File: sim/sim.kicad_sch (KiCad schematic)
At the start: 25 parts, among them Q1 BC817, Q2 BC807, Q3 BUK7880-55A, U1 AD8051, U2 AD8051, U3 LM393

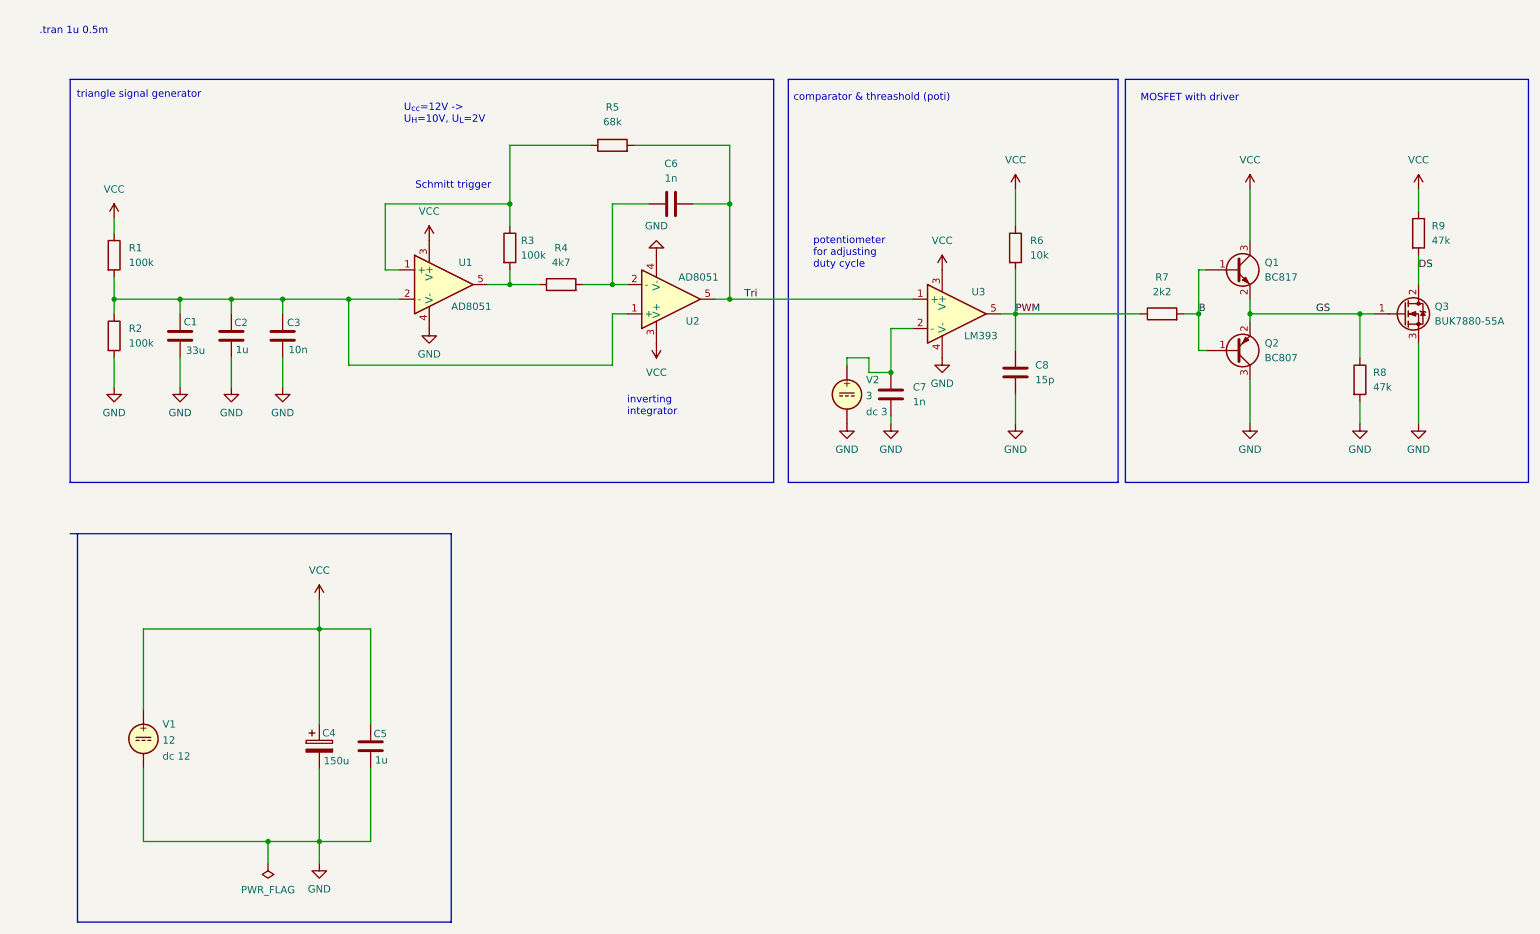
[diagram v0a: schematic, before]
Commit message: simulation model error fix
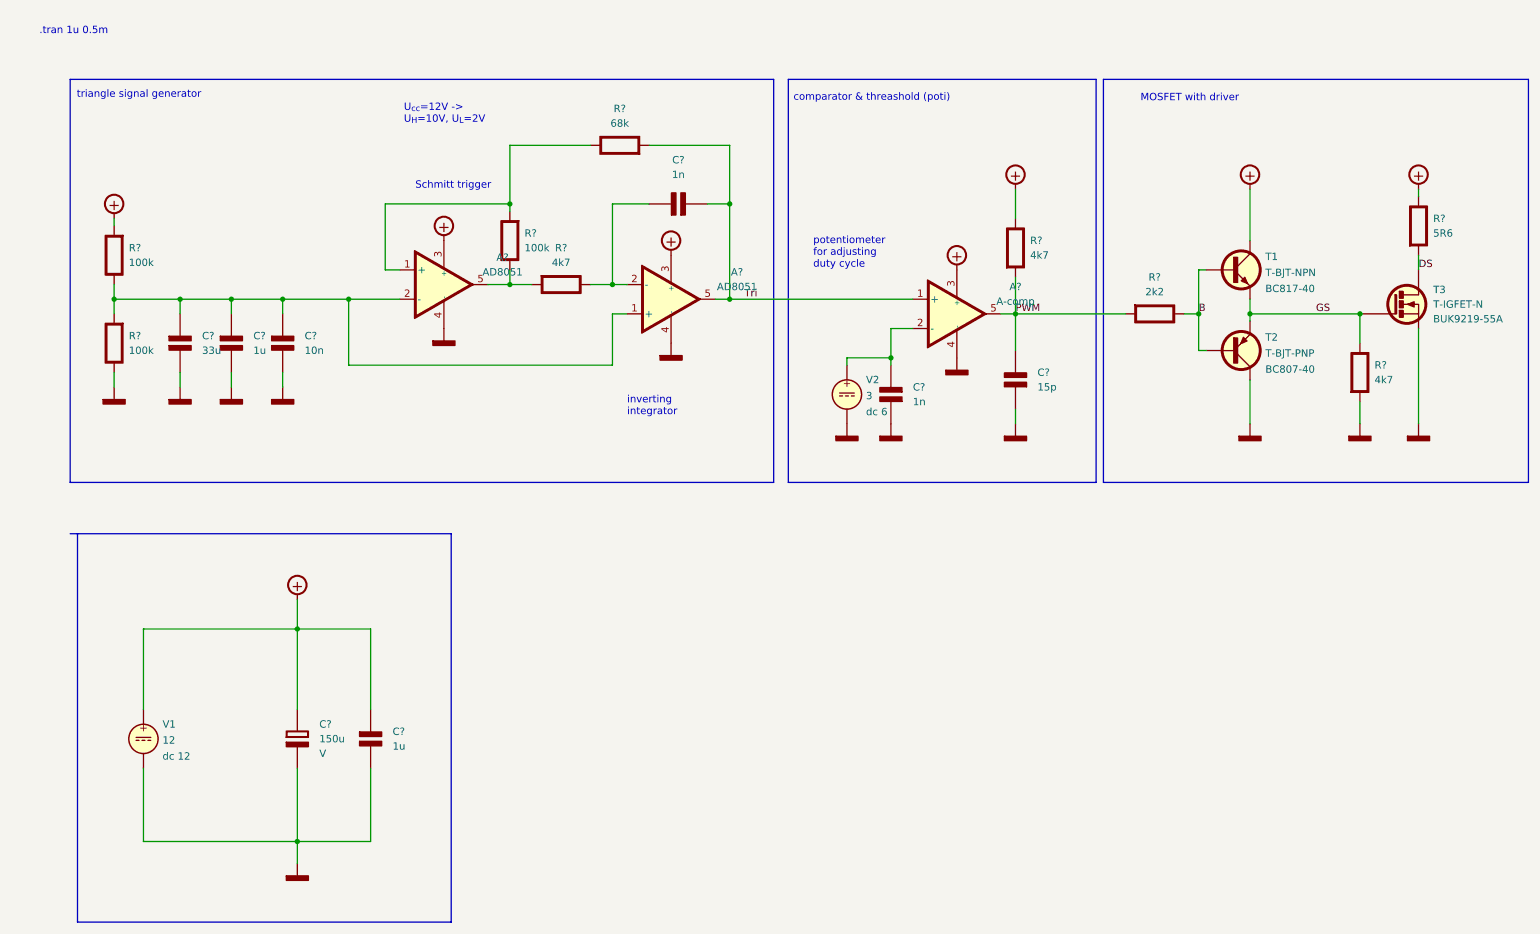
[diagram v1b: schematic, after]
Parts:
- removed C1: 33u, Capacitor_SMD:C_1206_3216Metric_Pad1.33x1.80mm_HandSolder, symbol Device:C
- removed C2, C5: 1u, Capacitor_SMD:C_1206_3216Metric_Pad1.33x1.80mm_HandSolder, symbol Device:C
- removed C3: 10n, Capacitor_SMD:C_1206_3216Metric_Pad1.33x1.80mm_HandSolder, symbol Device:C
- removed C4: 150u, Capacitor_THT:CP_Radial_D6.3mm_P2.50mm, symbol Device:C_Polarized
- removed C6, C7: 1n, Capacitor_SMD:C_1206_3216Metric_Pad1.33x1.80mm_HandSolder, symbol Device:C
- removed C8: 15p, Capacitor_SMD:C_1206_3216Metric_Pad1.33x1.80mm_HandSolder, symbol Device:C
- removed Q1: BC817, Package_TO_SOT_SMD:SOT-23, symbol Transistor_BJT:BC817
- removed Q2: BC807, Package_TO_SOT_SMD:SOT-23, symbol Transistor_BJT:BC807
- removed Q3: BUK7880-55A, Package_TO_SOT_SMD:SOT-223-3_TabPin2, symbol Transistor_FET:BUK7880-55A
- removed R1, R2, R3: 100k, Resistor_SMD:R_1206_3216Metric_Pad1.30x1.75mm_HandSolder, symbol Device:R
- removed R4: 4k7, Resistor_SMD:R_1206_3216Metric_Pad1.30x1.75mm_HandSolder, symbol Device:R
- removed R5: 68k, Resistor_SMD:R_1206_3216Metric_Pad1.30x1.75mm_HandSolder, symbol Device:R
- removed R6: 10k, Resistor_SMD:R_1206_3216Metric_Pad1.30x1.75mm_HandSolder, symbol Device:R
- removed R7: 2k2, Resistor_SMD:R_1206_3216Metric_Pad1.30x1.75mm_HandSolder, symbol Device:R
- removed R8, R9: 47k, Resistor_SMD:R_1206_3216Metric_Pad1.30x1.75mm_HandSolder, symbol Device:R
- removed U1, U2: AD8051, symbol sallen_key_schlib:Generic_Opamp
- removed U3: LM393, symbol sallen_key_schlib:Generic_Opamp
- added A?: A-comp, symbol Elektuur:A-comp
- added A?: AD8051, symbol Elektuur:A-comp
- added A?: AD8051, symbol Elektuur:A-opamp
- added C?: 15p, symbol Elektuur:C
- added C? (x2): 1u, symbol Elektuur:C
- added C? (x2): 1n, symbol Elektuur:C
- added C?: 150u, symbol Elektuur:C-polar
- added C?: 33u, symbol Elektuur:C
- added C?: 10n, symbol Elektuur:C
- added R? (x3): 100k, symbol Elektuur:R
- added R?: 5R6, symbol Elektuur:R
- added R? (x3): 4k7, symbol Elektuur:R
- added R?: 68k, symbol Elektuur:R
- added R?: 2k2, symbol Elektuur:R
- added T1: T-BJT-NPN, symbol Elektuur:T-BJT-NPN
- added T2: T-BJT-PNP, symbol Elektuur:T-BJT-PNP
- added T3: T-IGFET-N, symbol Elektuur:T-IGFET-N
- V2: Spice_Model dc 3 -> dc 6
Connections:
- net B: now also R?.1 (+), T1.2 (B), T2.2 (B)
- net DS: now also R?.2 (-), T3.1 (D)
- net GS: now also R?.1 (+), T1.3 (E), T2.3 (E), T3.2 (G)
- net PWM: now also A?.5 (OUT), C?.2 (-), R?.2 (-), R?.2 (-)
- net Tri: now also A?.1 (+), A?.5 (OUT), C?.2 (-), R?.2 (-)
- net at V2.1: now also A?.2 (-), C?.2 (-)
- net GND renamed 0
- net 0: now also A?.4 (-), A?.4 (-), A?.4 (-), C?.1 (+), C?.1 (+), C?.2 (-), C?.2 (-), C?.2 (-), C?.2 (-), C?.2 (-), R?.1 (+), R?.2 (-), T2.1 (C), T3.3 (S)
- net VCC renamed +
- net +: now also A?.3 (+), A?.3 (+), A?.3 (+), C?.1 (+), C?.1 (+), R?.1 (+), R?.1 (+), R?.2 (-), T1.1 (C)
- new net: A?.1 (+), A?.2 (-), C?.1 (+), C?.1 (+), C?.1 (+), R?.1 (+), R?.2 (-)
- new net: A?.2 (-), C?.1 (+), R?.1 (+)
- new net: A?.5 (OUT), R?.1 (+), R?.2 (-)
- new net: A?.1 (+), R?.1 (+), R?.2 (-)

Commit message: cleaning
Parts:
- R6: renamed from R?; value 4k7 -> 4k9
- V1: Spice_Model dc 12 -> dc 12 ac 0
- V2: value 3 -> 6; Spice_Model dc 6 -> dc 6 ac 0
- gave numbers to parts that had none: 19
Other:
- note added: ".tran 1u 0.5m .options gmin=1e-10 .options abstol=1e-10 .options reltol=0.003 .options cshunt=1e-15"
- note removed: ".tran 1u 0.5m"
- company: (none) -> Cherrytree
- title: (none) -> PWM generator simulation
- moved on the sheet: C6, C7, V2

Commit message: some more simulation stuff
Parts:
- A1, A2: value AD8051 -> TLV2371
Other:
- moved on the sheet: R6
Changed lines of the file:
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@@
   (junction (at 100.33 62.23) (diameter 0) (color 0 0 0 0)
   )
-  (junction (at 100.33 48.26) (diameter 0) (color 0 0 0 0)
+  (junction (at 100.33 38.1) (diameter 0) (color 0 0 0 0)
   )
   (junction (at 228.6 67.31) (diameter 0) (color 0 0 0 0)
@@
     (stroke (width 0) (type default) (color 0 0 0 0))
   )
-  (wire (pts (xy 100.33 48.26) (xy 78.74 48.26))
+  (wire (pts (xy 100.33 38.1) (xy 78.74 38.1))
     (stroke (width 0) (type default) (color 0 0 0 0))
   )
@@
     (stroke (width 0) (type default) (color 0 0 0 0))
   )
-  (wire (pts (xy 187.96 45.72) (xy 187.96 50.8))
+  (wire (pts (xy 187.96 45.72) (xy 187.96 46.99))
     (stroke (width 0) (type default) (color 0 0 0 0))
   )
@@
     (stroke (width 0) (type default) (color 0 0 0 0))
   )
-  (wire (pts (xy 100.33 49.53) (xy 100.33 48.26))
+  (wire (pts (xy 100.33 49.53) (xy 100.33 38.1))
     (stroke (width 0) (type default) (color 0 0 0 0))
   )
@@
     (stroke (width 0) (type default) (color 0 0 0 0))
   )
-  (wire (pts (xy 100.33 38.1) (xy 100.33 48.26))
-    (stroke (width 0) (type default) (color 0 0 0 0))
-  )
   (polyline (pts (xy 146.05 26.67) (xy 146.05 96.52))
     (stroke (width 0) (type default) (color 0 0 0 0))
@@
     (stroke (width 0) (type default) (color 0 0 0 0))
   )
-  (wire (pts (xy 78.74 48.26) (xy 78.74 59.69))
-    (stroke (width 0) (type default) (color 0 0 0 0))
-  )
-  (wire (pts (xy 187.96 60.96) (xy 187.96 67.31))
+  (wire (pts (xy 78.74 38.1) (xy 78.74 59.69))
+    (stroke (width 0) (type default) (color 0 0 0 0))
+  )
+  (wire (pts (xy 187.96 57.15) (xy 187.96 67.31))
     (stroke (width 0) (type default) (color 0 0 0 0))
   )
@@
     (effects (font (size 1.27 1.27)) (justify left bottom))
   )
-  (text "Schmitt trigger" (at 83.947 45.847 0)
+  (text "Schmitt trigger" (at 82.55 45.72 0)
     (effects (font (size 1.27 1.27)) (justify left bottom))
   )
@@
   )
   (symbol (lib_id "Elektuur:A-comp") (at 177.8 67.31 0) (unit 1)
-    (in_bom yes) (on_board yes) (fields_autoplaced)
-    (property "Reference" "A3" (id 0) (at 187.96 62.611 0))
-    (property "Value" "A-comp" (id 1) (at 187.96 65.151 0))
+    (in_bom yes) (on_board yes)
+    (property "Reference" "A3" (id 0) (at 184.15 69.85 0))
+    (property "Value" "A-comp" (id 1) (at 182.88 72.39 0))
     (property "Footprint" "" (id 2) (at 177.8 67.31 0)
       (effects (font (size 1.27 1.27)) hide)
@@
       (effects (font (size 1.27 1.27)) (justify left) hide)
     )
-    (property "Spice_Model" "LM393" (id 5) (at 177.8 67.31 0)
-      (effects (font (size 1.27 1.27)) hide)
-    )
+    (property "Spice_Model" "LM393" (id 5) (at 177.8 67.31 0))
     (property "Spice_Netlist_Enabled" "Y" (id 6) (at 177.8 67.31 0)
       (effects (font (size 1.27 1.27)) hide)
@@
   )
   (symbol (lib_id "Elektuur:A-comp") (at 88.9 62.23 0) (unit 1)
-    (in_bom yes) (on_board yes) (fields_autoplaced)
-    (property "Reference" "A1" (id 0) (at 99.06 57.531 0))
-    (property "Value" "AD8051" (id 1) (at 99.06 60.071 0))
+    (in_bom yes) (on_board yes)
+    (property "Reference" "A1" (id 0) (at 95.25 64.77 0))
+    (property "Value" "TLV2371" (id 1) (at 95.25 67.31 0))
     (property "Footprint" "" (id 2) (at 88.9 62.23 0)
       (effects (font (size 1.27 1.27)) hide)
@@
       (effects (font (size 1.27 1.27)) (justify left) hide)
     )
-    (property "Spice_Model" "AD8051" (id 5) (at 88.9 62.23 0)
-      (effects (font (size 1.27 1.27)) hide)
-    )
+    (property "Spice_Model" "AD8051" (id 5) (at 88.9 62.23 0))
     (property "Spice_Netlist_Enabled" "Y" (id 6) (at 88.9 62.23 0)
       (effects (font (size 1.27 1.27)) hide)
@@
     (pin "0")
   )
-  (symbol (lib_id "Elektuur:R") (at 187.96 55.88 0) (unit 1)
-    (in_bom yes) (on_board yes) (fields_autoplaced)
-    (property "Reference" "R6" (id 0) (at 190.5 54.6099 0)
-      (effects (font (size 1.27 1.27)) (justify left))
-    )
-    (property "Value" "4k9" (id 1) (at 190.5 57.1499 0)
-      (effects (font (size 1.27 1.27)) (justify left))
-    )
-    (property "Footprint" "" (id 2) (at 187.96 55.88 0)
-      (effects (font (size 1.27 1.27)) hide)
-    )
-    (property "Datasheet" "" (id 3) (at 187.96 55.88 0)
-      (effects (font (size 1.27 1.27)) hide)
-    )
-    (property "Indicator" "+" (id 4) (at 184.785 52.705 0)
-      (effects (font (size 1.27 1.27)) hide)
-    )
-    (property "Rating" "W" (id 5) (at 190.5 59.055 0)
+  (symbol (lib_id "Elektuur:R") (at 187.96 52.07 0) (unit 1)
+    (in_bom yes) (on_board yes) (fields_autoplaced)
+    (property "Reference" "R6" (id 0) (at 190.5 50.7999 0)
+      (effects (font (size 1.27 1.27)) (justify left))
+    )
+    (property "Value" "4k9" (id 1) (at 190.5 53.3399 0)
+      (effects (font (size 1.27 1.27)) (justify left))
+    )
+    (property "Footprint" "" (id 2) (at 187.96 52.07 0)
+      (effects (font (size 1.27 1.27)) hide)
+    )
+    (property "Datasheet" "" (id 3) (at 187.96 52.07 0)
+      (effects (font (size 1.27 1.27)) hide)
+    )
+    (property "Indicator" "+" (id 4) (at 184.785 48.895 0)
+      (effects (font (size 1.27 1.27)) hide)
+    )
+    (property "Rating" "W" (id 5) (at 190.5 55.245 0)
       (effects (font (size 1.27 1.27)) (justify left) hide)
     )
@@
   )
   (symbol (lib_id "Elektuur:A-opamp") (at 128.27 64.77 0) (unit 1)
-    (in_bom yes) (on_board yes) (fields_autoplaced)
-    (property "Reference" "A2" (id 0) (at 139.7 60.071 0))
-    (property "Value" "AD8051" (id 1) (at 139.7 62.611 0))
+    (in_bom yes) (on_board yes)
+    (property "Reference" "A2" (id 0) (at 134.62 67.31 0))
+    (property "Value" "TLV2371" (id 1) (at 134.62 69.85 0))
     (property "Footprint" "" (id 2) (at 128.27 64.77 0)
       (effects (font (size 1.27 1.27)) hide)
@@
       (effects (font (size 1.27 1.27)) (justify left) hide)
     )
-    (property "Spice_Model" "AD8051" (id 5) (at 128.27 64.77 0)
-      (effects (font (size 1.27 1.27)) hide)
-    )
+    (property "Spice_Model" "AD8051" (id 5) (at 128.27 64.77 0))
     (property "Spice_Netlist_Enabled" "Y" (id 6) (at 128.27 64.77 0)
       (effects (font (size 1.27 1.27)) hide)
@@
     )
     (path "/7edbef52-719a-4d33-9d4c-a08d64073863"
-      (reference "A1") (unit 1) (value "AD8051") (footprint "")
+      (reference "A1") (unit 1) (value "TLV2371") (footprint "")
     )
     (path "/c507f812-25fc-46e2-816c-f3c8f6ee17ec"
-      (reference "A2") (unit 1) (value "AD8051") (footprint "")
+      (reference "A2") (unit 1) (value "TLV2371") (footprint "")
     )
     (path "/0dce3ede-e8fb-4eb0-881b-c68a5e81702d"
